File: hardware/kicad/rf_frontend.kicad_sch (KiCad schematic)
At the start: 27 parts, among them J2 SMA/EDGE(ANT), U10 NA(PE42522B), U12 LFCN-2250+(FV1206), U13 LNA_MMIC(TBD,~100mA), U6 PE42522B(LGA29), U7 PE42522B(LGA29), U9 NA(PE42522B)

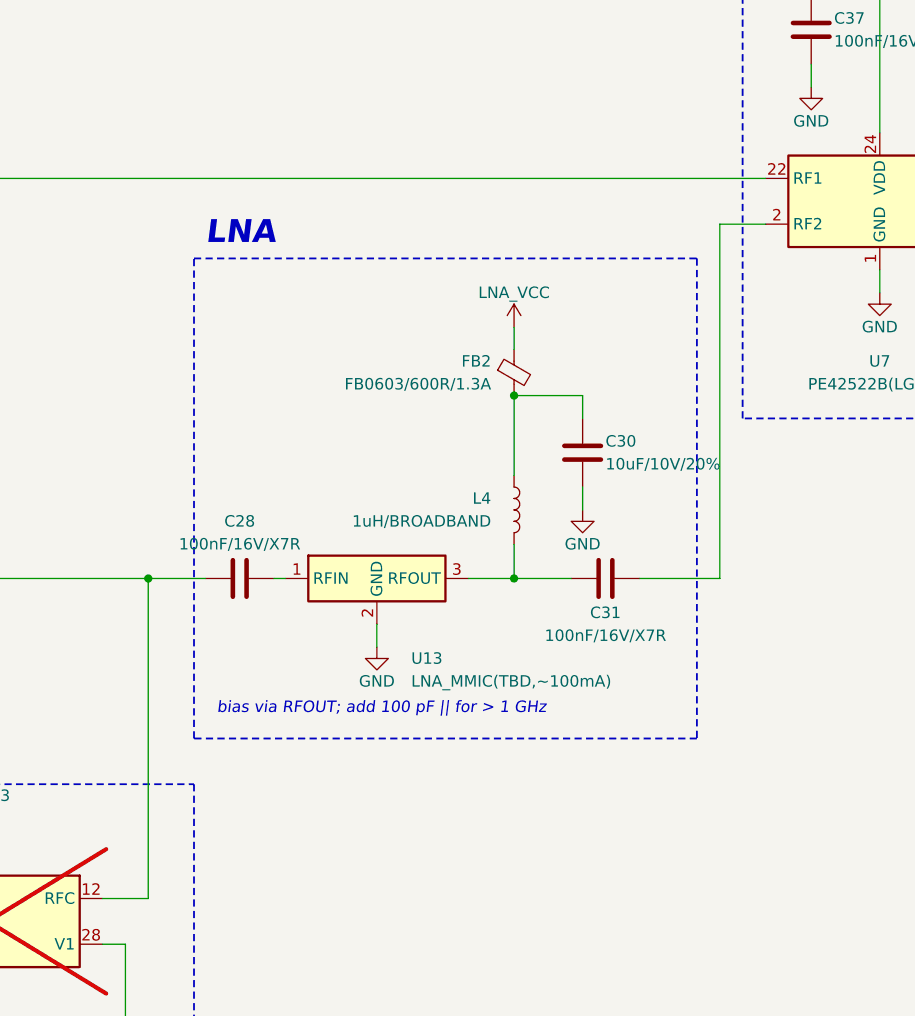
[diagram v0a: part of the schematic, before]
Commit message: Schematic: QPL9547 LNA, Arial font
- U13 is the Qorvo QPL9547 (DFN-8 2x2): VDD through the RF_OUT choke,
  R25 sets the bias at VBIAS, R26 holds SHDN low (VERIFY items).
- All schematic text uses the Arial TrueType face.
- Docs and generator comments updated.

Co-Authored-By: Claude Opus 5.5 <noreply@anthropic.com>
Claude-Session: https://claude.ai/code/session_01YRUiF8Vp4242sya9Xyg3TV
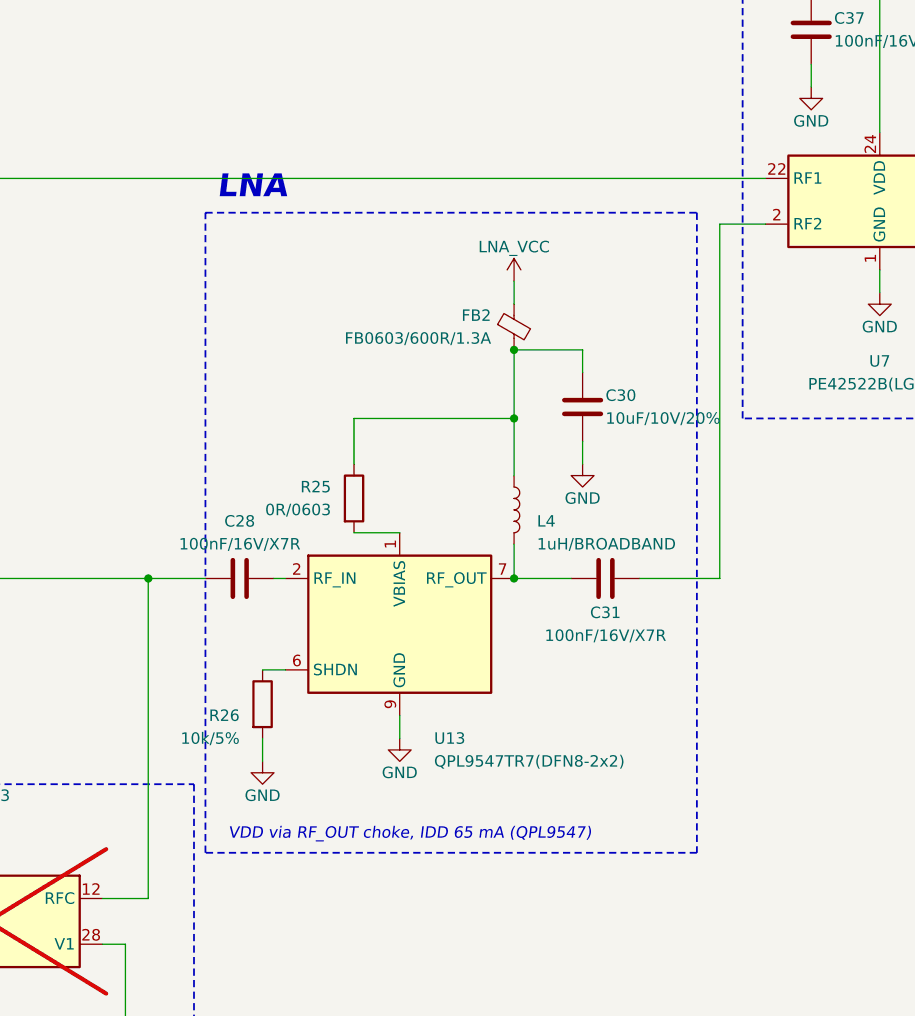
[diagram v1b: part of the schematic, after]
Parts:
- removed U13: LNA_MMIC(TBD,~100mA), coaxolotl:LNA_TBD, symbol coaxolotl:LNA_MMIC
- added R25: 0R/0603, Resistor_SMD:R_0603_1608Metric, symbol Device:R
- added R26: 10k/5%, Resistor_SMD:R_0603_1608Metric, symbol Device:R
- added U13: QPL9547TR7(DFN8-2x2), coaxolotl:Qorvo_DFN-8-1EP_2x2mm_P0.5mm, symbol coaxolotl:QPL9547
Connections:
- net GND: now also R26.2, U13.9 (GND)
- net at C30.1, FB2.2, L4.1: now also R25.1
- net at C31.1, L4.2: now also U13.7 (RF_OUT)
- net at C28.2: now also U13.2 (RF_IN)
- new net: R25.2, U13.1 (VBIAS)
- new net: R26.1, U13.6 (SHDN)
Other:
- note added: "VDD via RF_OUT choke, IDD 65 mA (QPL9547)"
- note removed: "bias via RFOUT; add 100 pF || for > 1 GHz"

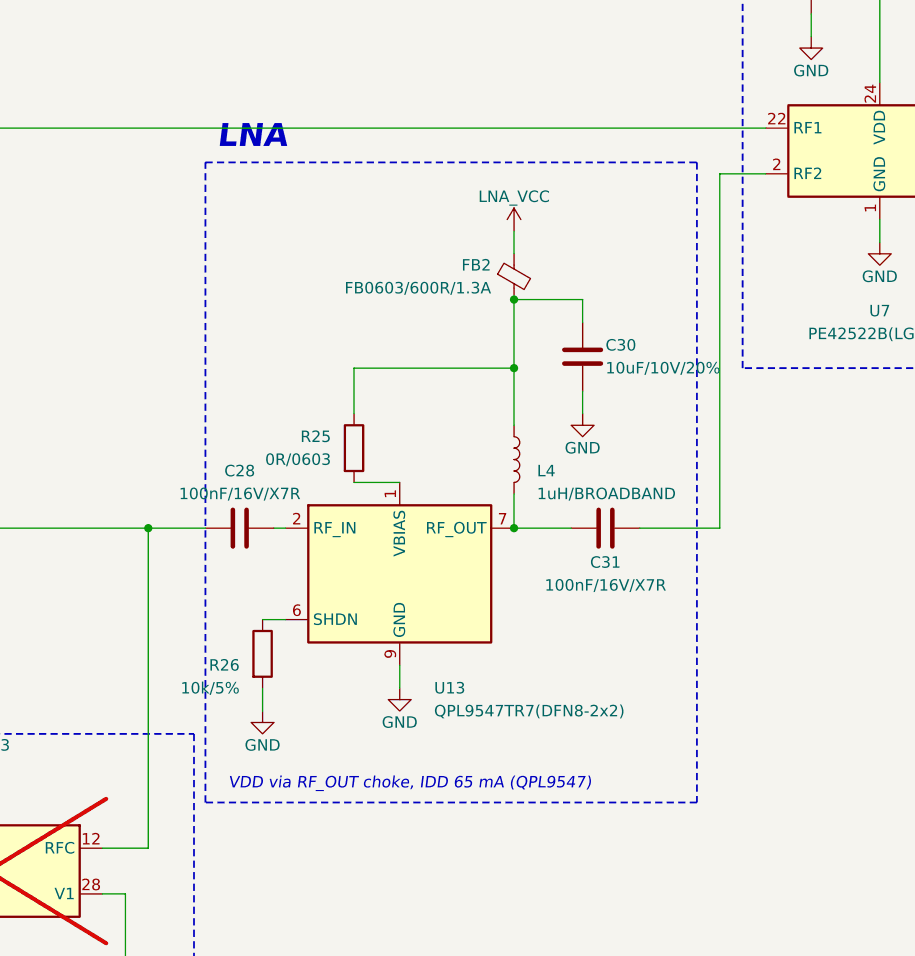
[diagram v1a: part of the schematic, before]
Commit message: LNA stage follows the SWL434 Spacewalker LNA
QPL9547: VBIAS via 3k32 + 100 pF, VDD into RF_OUT via 560 nH, 100 pF,
ferrite bead, 100 pF; SHDN and NC 4/5/8 to GND. DC blocks 1 nF C0G for
the 25 MHz lower edge.

Co-Authored-By: Claude Opus 5.5 <noreply@anthropic.com>
Claude-Session: https://claude.ai/code/session_01YRUiF8Vp4242sya9Xyg3TV
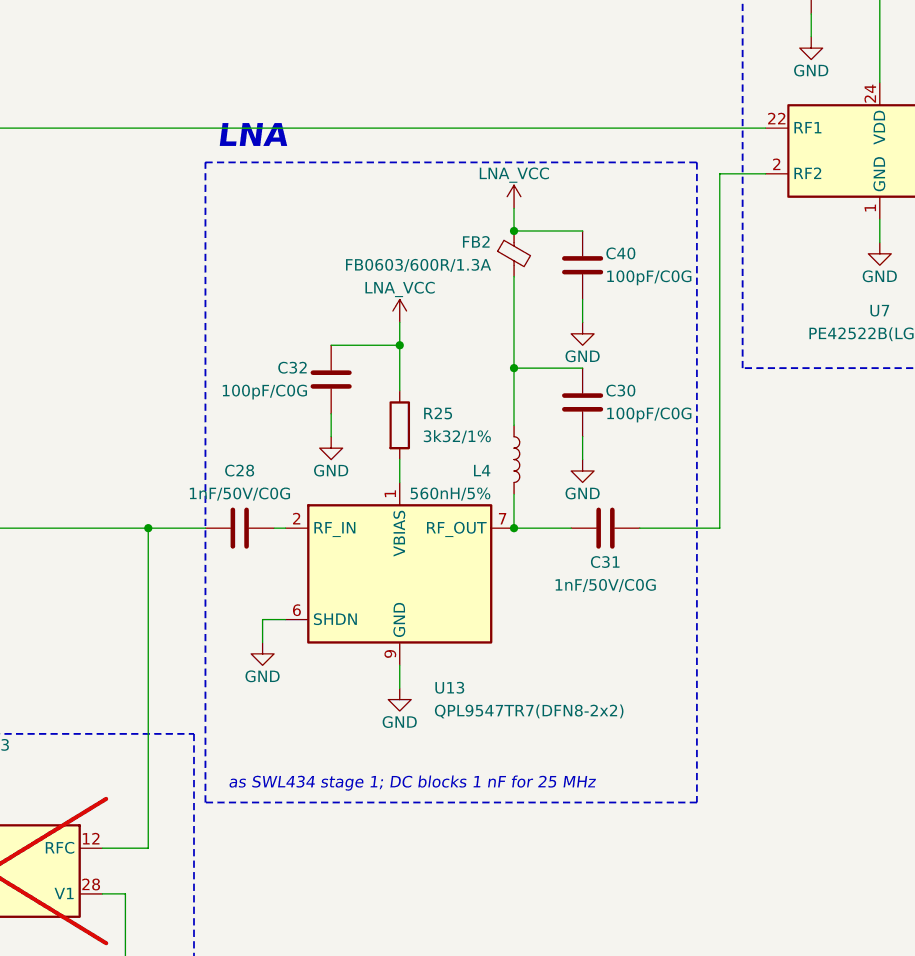
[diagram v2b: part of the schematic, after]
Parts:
- removed R26: 10k/5%, Resistor_SMD:R_0603_1608Metric, symbol Device:R
- added C32, C40: 100pF/C0G, Capacitor_SMD:C_0603_1608Metric, symbol Device:C
- C28, C31: value 100nF/16V/X7R -> 1nF/50V/C0G
- C30: value 10uF/10V/20% -> 100pF/C0G; footprint Capacitor_SMD:C_0805_2012Metric -> Capacitor_SMD:C_0603_1608Metric
- L4: value 1uH/BROADBAND -> 560nH/5%; footprint Inductor_SMD:L_0805_2012Metric -> Inductor_SMD:L_0603_1608Metric; Note VERIFY SRF > 2 GHz or conical -> (none)
- R25: value 0R/0603 -> 3k32/1%; Note Rbias: sets IDD (65 mA default) -> sets IDD (SWL434: 3k32 @ 5 V)
- U13: Note VERIFY Rbias / SHDN polarity / RF_OUT choke against the dat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 -> (none)
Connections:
- net GND: now also U13.4 (GND), U13.5 (GND), U13.6 (SHDN), U13.8 (GND), C32.2, C40.2
- net LNA_VCC: now also R25.1, C32.1, C40.1
- net at C30.1, FB2.2, L4.1: no longer R25.1
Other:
- note added: "as SWL434 stage 1; DC blocks 1 nF for 25 MHz"
- note removed: "VDD via RF_OUT choke, IDD 65 mA (QPL9547)"

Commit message: Schematic: PE42520 SPDTs instead of PE42522
PE42520C-Z (QFN-16 3x3, LCSC C500478) pinout and truth table checked
against the LCSC datasheet: LS tied to VDD so CTRL = 0 selects RF1
(bypass) and the firmware stays unchanged. KiCad library footprint
QFN-16-1EP_3x3mm_P0.5mm_EP1.7x1.7mm.

Co-Authored-By: Claude Opus 5.5 <noreply@anthropic.com>
Claude-Session: https://claude.ai/code/session_01YRUiF8Vp4242sya9Xyg3TV
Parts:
- removed U10, U9: NA(PE42522B), coaxolotl:PE42522_LGA-29_4x4mm, symbol coaxolotl:PE42522
- removed U6, U7: PE42522B(LGA29), coaxolotl:PE42522_LGA-29_4x4mm, symbol coaxolotl:PE42522
- added U10, U9: NA(PE42520C-Z), Package_DFN_QFN:QFN-16-1EP_3x3mm_P0.5mm_EP1.7x1.7mm, symbol coaxolotl:PE42520
- added U6, U7: PE42520C-Z(QFN16), Package_DFN_QFN:QFN-16-1EP_3x3mm_P0.5mm_EP1.7x1.7mm, symbol coaxolotl:PE42520
- C36: Place U6.24 -> U6.16
- C37: Place U7.24 -> U7.16
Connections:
- net +3V3: now also U10.15 (LS), U10.16 (VDD), U6.15 (LS), U6.16 (VDD), U7.15 (LS), U7.16 (VDD), U9.15 (LS), U9.16 (VDD)
- net FMN: now also U10.14 (CTRL), U9.14 (CTRL)
- net GND: now also U10.1 (GND), U10.10 (GND), U10.12 (GND), U10.13 (GND), U10.17 (GND), U10.3 (GND), U10.4 (GND), U10.5 (GND), U10.6 (GND), U10.8 (GND), U10.9 (GND), U6.1 (GND), U6.10 (GND), U6.12 (GND), U6.13 (GND), U6.17 (GND), U6.3 (GND), U6.4 (GND), U6.5 (GND), U6.6 (GND), U6.8 (GND), U6.9 (GND), U7.1 (GND), U7.10 (GND), U7.12 (GND), U7.13 (GND), U7.17 (GND), U7.3 (GND), U7.4 (GND), U7.5 (GND), U7.6 (GND), U7.8 (GND), U7.9 (GND), U9.1 (GND), U9.10 (GND), U9.12 (GND), U9.13 (GND), U9.17 (GND), U9.3 (GND), U9.4 (GND), U9.5 (GND), U9.6 (GND), U9.8 (GND), U9.9 (GND)
- net LNA_PATH: now also U6.14 (CTRL), U7.14 (CTRL)
- net RF_BANK: now also U7.7 (RFC)
- net at D6.3 (K), GDT1.3, J2.1 (In)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: now also U6.7 (RFC)
- net at C24.1: now also U6.11 (RF2)
- net at C27.1, L3.1: now also U9.11 (RF2)
- net at C27.2, L3.2: now also U10.11 (RF2)
- net at C28.1, R22.2: now also U10.7 (RFC)
- net at C31.2: now also U7.11 (RF2)
- net at R22.1, U12.3 (OUT): now also U9.7 (RFC)
- new net: U6.2 (RF1), U7.2 (RF1)
- new net: U10.2 (RF1), U9.2 (RF1)
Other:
- note added: "PE42520 RF ports sit at 0 VDC: no blocking caps except around the LNA."
- note removed: "PE42522 RF ports sit at 0 VDC: no blocking caps except around the LNA."

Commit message: QPL9547: datasheet footprint (DFN-8 2x2, EP 0.8x1.6), LCSC C5367093
Datasheet rev D checked: pads 1 VBIAS, 2 RF in, 6 shutdown (low/ground =
on), 7 RF out + VDD, 3/4/5/8 NC (grounded as on the SWL434), paddle GND;
R4 3k32 sets IDD = 65 mA, same as R25. KiCad library footprint
DFN-8-1EP_2x2mm_P0.5mm_EP0.8x1.6mm matches the land pattern.

Co-Authored-By: Claude Opus 5.5 <noreply@anthropic.com>
Claude-Session: https://claude.ai/code/session_01YRUiF8Vp4242sya9Xyg3TV
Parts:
- U13: footprint coaxolotl:Qorvo_DFN-8-1EP_2x2mm_P0.5mm -> Package_DFN_QFN:DFN-8-1EP_2x2mm_P0.5mm_EP0.8x1.6mm; LCSC (none) -> C5367093; Note (none) -> EP: 0.25 mm vias under the paddle (datasheet p.8)

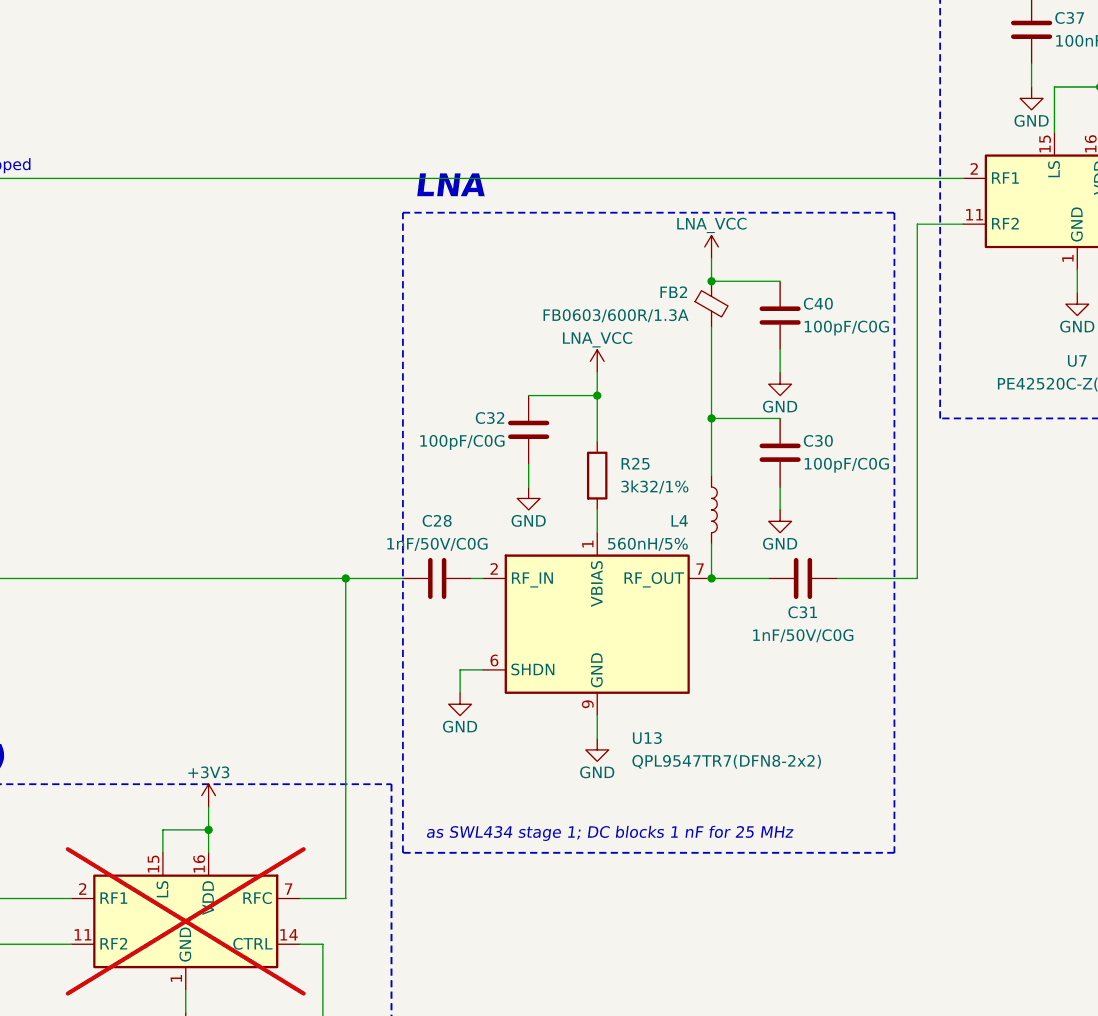
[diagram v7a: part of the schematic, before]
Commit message: LNA bias feed: 18 nH at RF_OUT (QPL9547 EVB) + 560 nH (SWL434)
The 560 nH 0603 choke is past its self-resonance above ~400 MHz; an
18 nH choke at the pin covers the GHz range, the 560 nH the low band.

Co-Authored-By: Claude Opus 5.5 <noreply@anthropic.com>
Claude-Session: https://claude.ai/code/session_01YRUiF8Vp4242sya9Xyg3TV
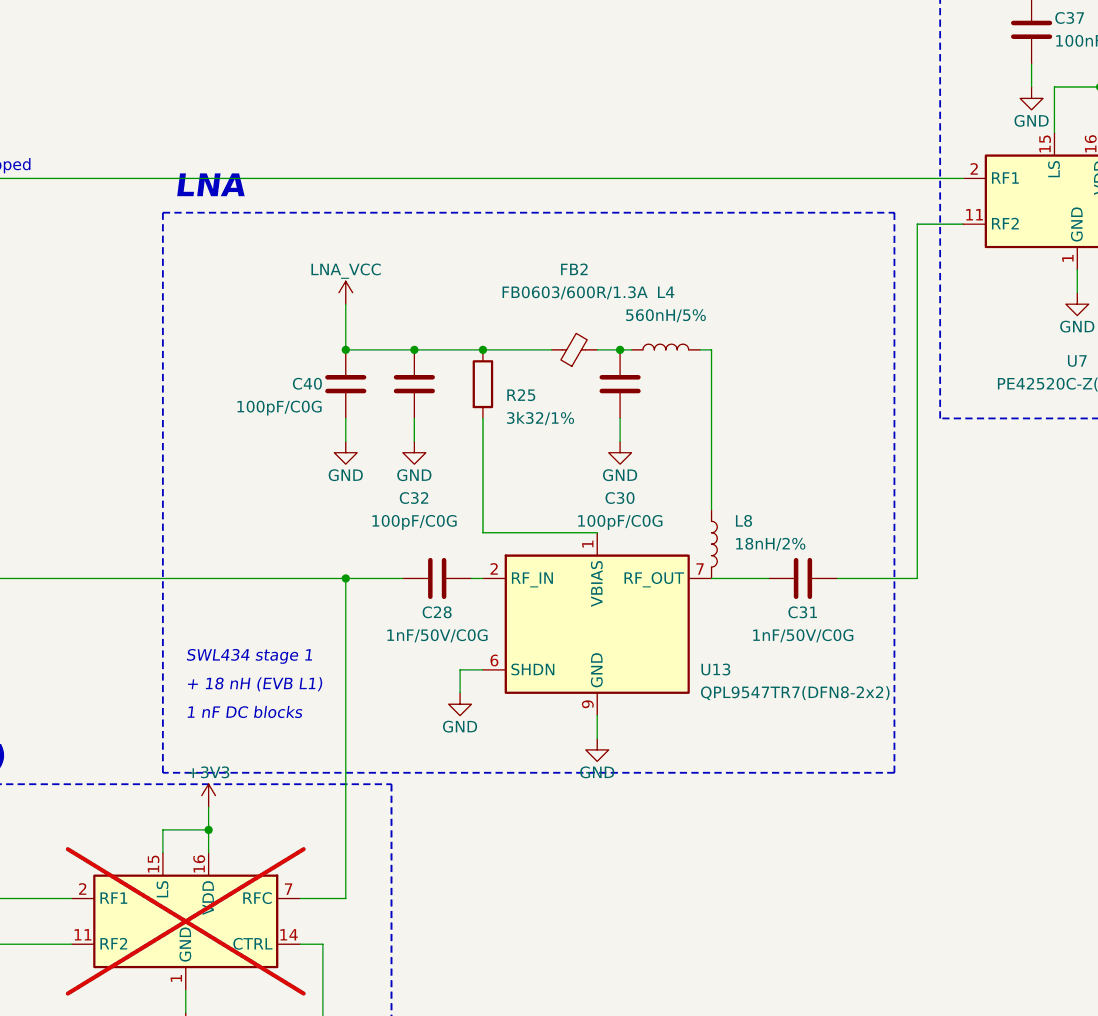
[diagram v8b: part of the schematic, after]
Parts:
- added L8: 18nH/2%, Inductor_SMD:L_0603_1608Metric, symbol Device:L
- L4: Note (none) -> low-band choke (SWL434)
- R25: Note sets IDD (SWL434: 3k32 @ 5 V) -> sets IDD = 65 mA (QPL9547 EVB R4)
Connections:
- net at C31.1, U13.7 (RF_OUT): now also L8.2; no longer L4.2
- new net: L4.2, L8.1
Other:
- note added: "+ 18 nH (EVB L1)"
- note added: "1 nF DC blocks"
- note added: "SWL434 stage 1"
- note removed: "as SWL434 stage 1; DC blocks 1 nF for 25 MHz"
